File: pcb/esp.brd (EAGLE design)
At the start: 37 x 61.5 mm, 28 parts, among them Q1 2N3904, Q2 2N3904

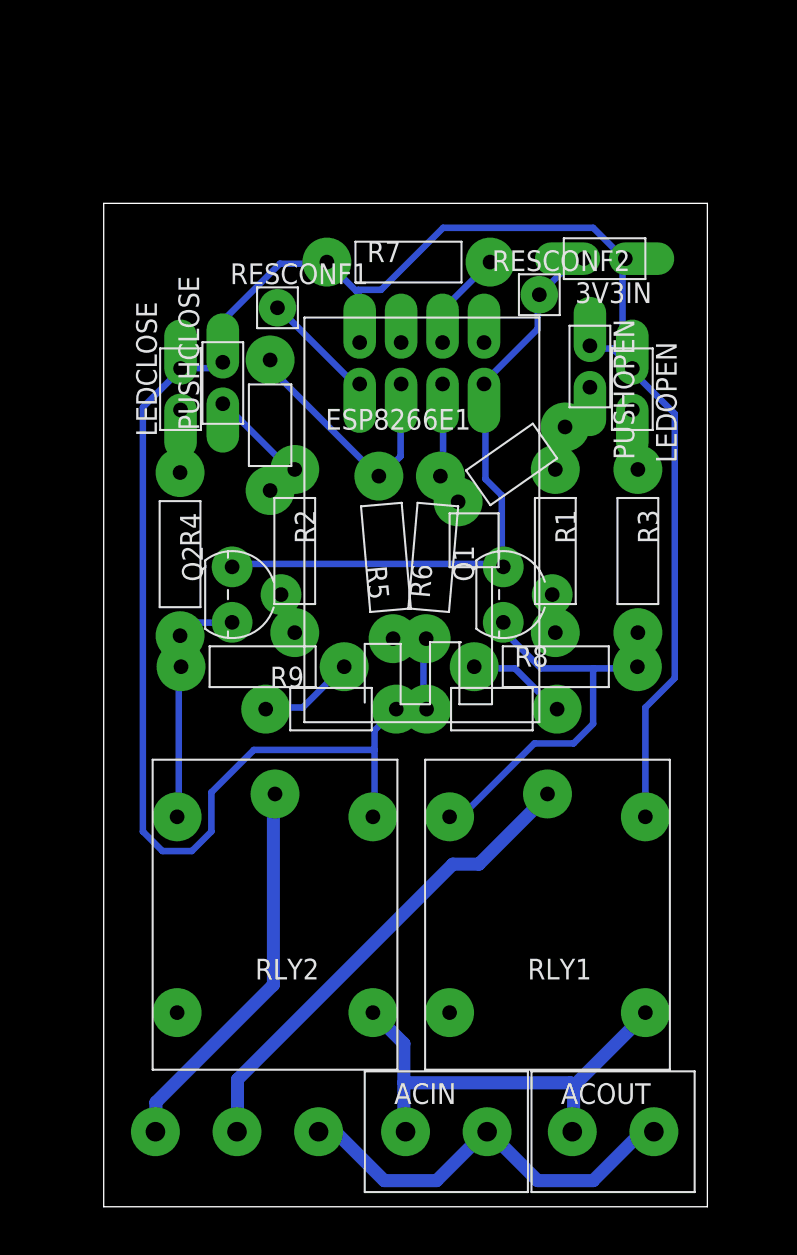
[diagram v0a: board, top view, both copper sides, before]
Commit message: Remove ignored EAGLE files. Separate the README files. Renew circuit schematic and board images.
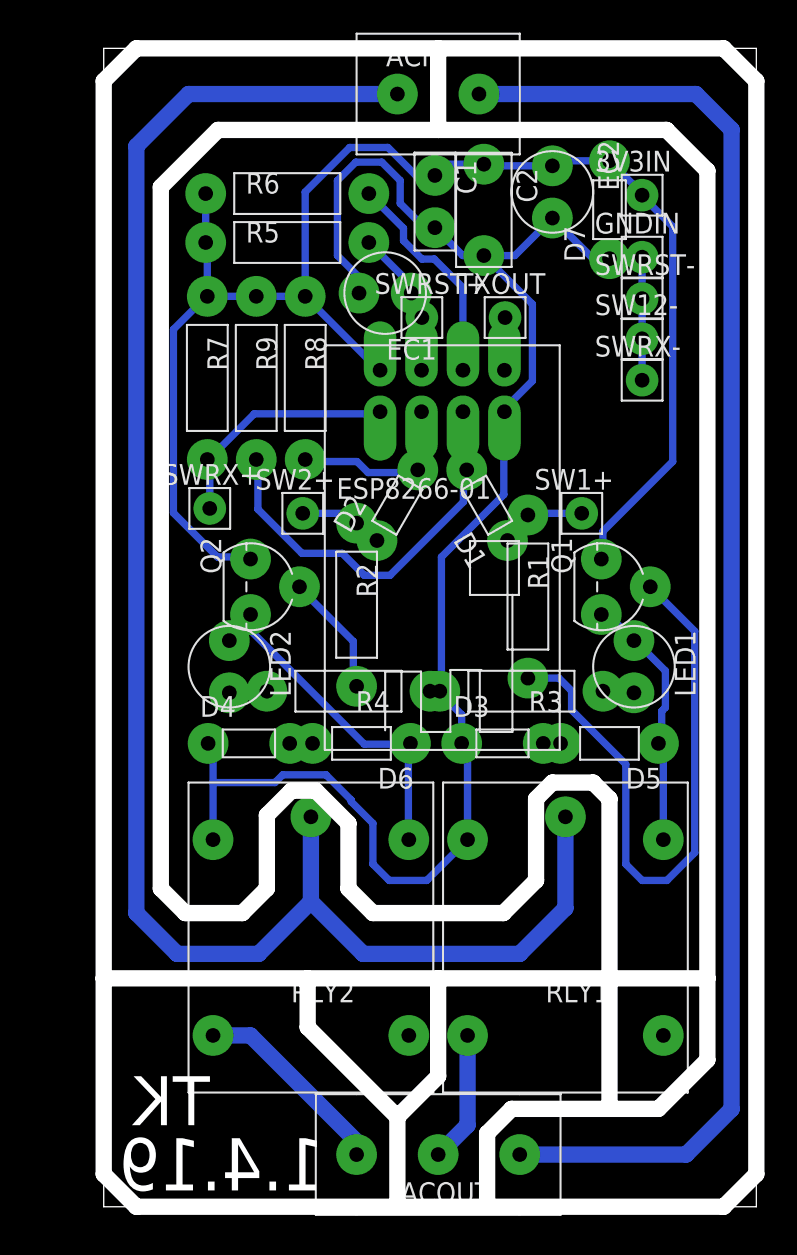
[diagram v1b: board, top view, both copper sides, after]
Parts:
- removed CURTAINOUT: CON3CON5.0S3T, simple-parts:CON5.0S3T
- removed ESP8266E1: ESP8266E01ESP8266E01, simple-parts:ESP8266E01
- removed LEDCLOSE, LEDOPEN, PUSHCLOSE, PUSHOPEN: PINPLUG2PINPLUG2, simple-parts:PINPLUG2
- removed RESCONF1, RESCONF2: PINPLUG1PINPLUG1, simple-parts:PINPLUG1
- added C1: 15pF, simple-parts:CERCAP3.2S
- added C2: 100nF, simple-parts:CERCAP5.6S
- added D5, D6, D7: 3V3, simple-parts:ZD6.0S2.0D
- added EC1: 100uF/16V, simple-parts:ECAP3.2S5.0D
- added EC2: 220uF/16V, simple-parts:ECAP3.2S5.0D
- added ESP8266-01: ESP8266E01ESP8266E01, simple-parts:ESP8266E01
- added GNDIN, SW1+, SW12-, SW2+, SWRST+, SWRST-, SWRX+, SWRX-, TXOUT: (no value), simple-parts:PINPLUG1
- added LED1, LED2: (no value), simple-parts:LED3.2S5.0D
- 3V3IN: value PINPLUG2PINPLUG2 -> (none); device simple-parts:PINPLUG2 -> simple-parts:PINPLUG1
- ACIN: value CON2CON5.0S2T -> (none)
- ACOUT: value CON2CON5.0S2T -> (none); device simple-parts:CON5.0S2T -> simple-parts:CON5.0S3T
- D1, D3: value 1N4007 -> 1N4148; device simple-parts:RD8.0S2.6D -> simple-parts:RD5.0S1.8D
- D2, D4: value 1N4001 -> 1N4148; device simple-parts:RD8.0S2.6D -> simple-parts:RD5.0S1.8D
- Q1, Q2: value 2N3904 -> 2N3906
- R1, R2: value 220R -> 470R
- R5, R6, R7: value 1K -> 3K3
- R8, R9: value 330R -> 2K2
- RLY1, RLY2: value (none) -> 3V3; device simple-parts:RLY12W12L -> simple-parts:RLY15W19L
- moved ACIN 63.6 mm to (20.5, 68.2)
- moved R6 24.0 mm to (11.2, 62.1), turned to 0 degrees
- moved R8 23.4 mm to (12.3, 50.8), turned to 270 degrees
- moved R5 20.2 mm to (11.2, 59.1), turned to 0 degrees
- moved D4 19.5 mm to (8.90, 28.4), turned to 0 degrees
- moved R9 17.7 mm to (9.35, 50.8), turned to 270 degrees
- moved R7 14.2 mm to (6.35, 50.8), turned to 270 degrees
- moved R4 13.3 mm to (15.0, 31.6), turned to 180 degrees
- moved D1 12.5 mm to (23.5, 43.0), turned to 120 degrees
- moved R3 11.2 mm to (25.6, 31.6), turned to 180 degrees
- moved ACOUT 10.8 mm to (20.5, 3.20), turned to 180 degrees
- moved D3 10.7 mm to (24.4, 28.4)
- moved D2 7.43 mm to (18.0, 43.0), turned to 60 degrees
- moved Q1 6.03 mm to (30.5, 38.0)
- moved R2 5.02 mm to (15.5, 36.9)
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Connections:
- removed net N$17 (its old number): D3.P+, R9.P$1
- removed net N$19: LEDCLOSE.P$1, R4.P$1
- removed net N$21: D1.P+, R8.P$1
- new net +3V3: 3V3IN.P$1, C1.P$1, C2.P$1, D7.P-, EC2.P+, ESP8266-01.VCC, Q1.3, Q2.3, R5.P$1, R6.P$1, R7.P$1, R8.P$1, R9.P$1
- new net GND: C1.P$2, C2.P$2, D3.P+, D4.P+, D7.P+, EC1.P-, EC2.P-, ESP8266-01.GND, GNDIN.P$1, R3.P$2, R4.P$1, RLY1.P$2, RLY2.P$2, SW12-.P$1, SWRST-.P$1, SWRX-.P$1
- new net N$18: D2.P+, R2.P$1, SW2+.P$1
- new net N$2: ESP8266-01.CH, R6.P$2
- new net N$23: D1.P-, ESP8266-01.IO2, R9.P$2
- net N$1: now also LED2.P-, R4.P$2; no longer Q1.1, R3.P$2, R8.P$2, RLY1.P$2
- net N$10: now also EC1.P+, ESP8266-01.RST, R5.P$2, SWRST+.P$1; no longer 3V3IN.P$1, D1.P-, D3.P-, ESP8266E1.VCC, LEDCLOSE.P$2, LEDOPEN.P$1, PUSHCLOSE.P$2, PUSHOPEN.P$1, R5.P$1, R6.P$1, R7.P$1, RLY1.P$1, RLY2.P$1
- net N$11: now also ACOUT.P$3, RLY2.NO; no longer D4.P-, PUSHCLOSE.P$1, R2.P$1
- net N$12: now also D5.P+, LED1.P+, Q1.1, RLY1.P$1; no longer D2.P+, ESP8266E1.GPIO2, R6.P$2
- net N$13: now also ESP8266-01.TX, TXOUT.P$1; no longer D4.P+, ESP8266E1.GPIO0, R5.P$2
- net N$14: now also D3.P-, D5.P-; no longer 3V3IN.P$2, ESP8266E1.GND, Q1.3, Q2.3, RESCONF2.P$1
- net N$15: now also ACOUT.P$2, RLY1.NO; no longer CURTAINOUT.P$3, RLY2.COM
- net N$16: now also ACIN.P$2, ACOUT.P$1; no longer CURTAINOUT.P$2, RLY1.COM
- net N$20: now also ACIN.P$1, RLY1.COM, RLY2.COM; no longer ESP8266E1.CH_PD, R7.P$2
- net N$3: now also ESP8266-01.RX, R7.P$2, SWRX+.P$1; no longer D2.P-, PUSHOPEN.P$2, R1.P$1
- net N$5: now also D1.P+, R1.P$1, SW1+.P$1; no longer LEDOPEN.P$2, R3.P$1
- net N$6: now also D2.P-, ESP8266-01.IO0, R8.P$2; no longer ACIN.P$2, ACOUT.P$2, CURTAINOUT.P$1
- net N$7: now also D6.P+, LED2.P+, RLY2.P$1; no longer R4.P$2, R9.P$2, RLY2.P$2
- net N$8: now also LED1.P-, R3.P$1; no longer ESP8266E1.RX, RESCONF1.P$1
- net N$9: now also D4.P-, D6.P-; no longer ACIN.P$1, ACOUT.P$1, RLY1.NO, RLY2.NO
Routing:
- net N$10: track 140.0 -> 9.18 mm
- net GND: track 0.00 -> 107.5 mm
- net N$20: track 6.13 -> 106.3 mm
- net +3V3: track 0.00 -> 94.1 mm
- net N$16: track 29.5 -> 90.6 mm
- net N$14: track 39.1 -> 1.06 mm
- net N$4: track 2.44 -> 37.8 mm
- net N$9: track 27.9 -> 1.40 mm
- net N$23: track 0.00 -> 24.9 mm
- net N$1: track 26.5 -> 2.34 mm
- net N$15: track 23.8 -> 8.05 mm
- net N$6: track 25.5 -> 11.0 mm
- net N$2: track 0.00 -> 13.7 mm
- net N$13: track 16.2 -> 3.25 mm
- net N$3: track 6.03 -> 14.9 mm
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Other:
- board size 37 x 61.5 mm -> 40 x 71 mm
- board text added: "1.4.19"
- board text added: "TK"
